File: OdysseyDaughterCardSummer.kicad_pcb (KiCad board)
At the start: 2 copper layers, 47.8 x 46.6 mm, 27 parts, among them J1 Conn_01x01, J2 Conn_01x01, J3 Conn_01x01, J4 Conn_01x01, X1 OdysseyDaughterCard

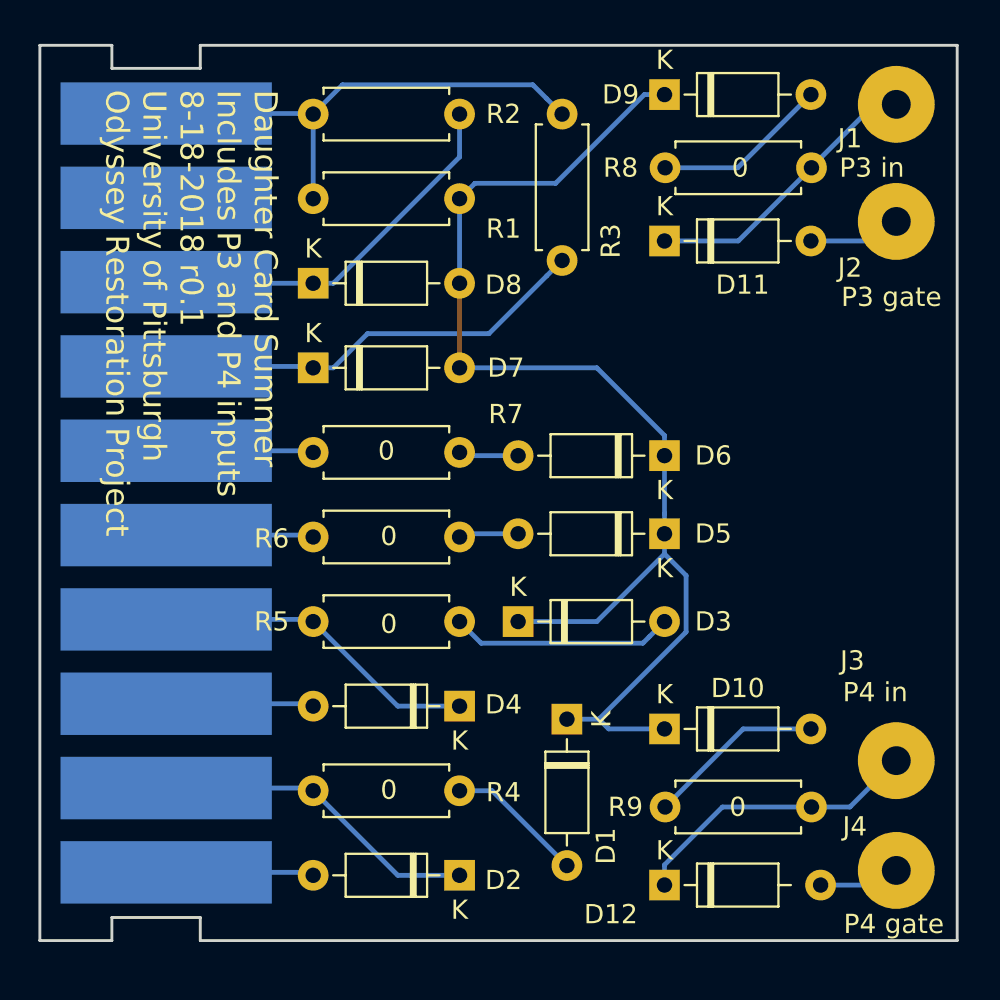
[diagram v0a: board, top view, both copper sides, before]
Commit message: R1.0 remove extra player hardware and replace with single port
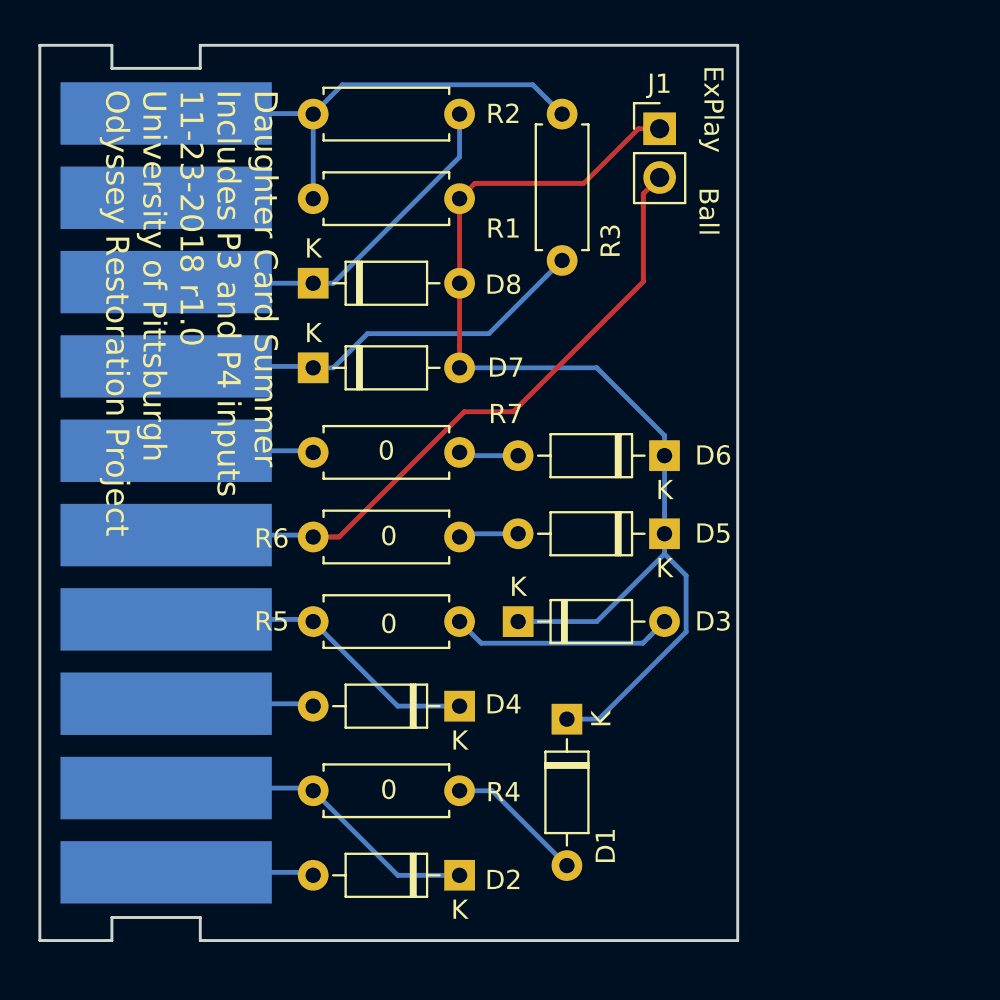
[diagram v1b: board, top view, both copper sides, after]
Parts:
- removed ?: , 
- removed D10, D9: 1N4448, Diode_THT:D_DO-35_SOD27_P7.62mm_Horizontal
- removed D11, D12: BAT83S, Diode_THT:D_DO-35_SOD27_P7.62mm_Horizontal
- removed J2, J3, J4: Conn_01x01, Connector_Wire:SolderWirePad_single_1-5mmDrill
- removed R8, R9: 0, Resistor_THT:R_Axial_DIN0207_L6.3mm_D2.5mm_P7.62mm_Horizontal
- J1: value Conn_01x01 -> Conn_01x02; footprint Connector_Wire:SolderWirePad_single_1-5mmDrill -> Connector_PinHeader_2.54mm:PinHeader_1x02_P2.54mm_Vertical
- moved J1 12.4 mm to (154.7, 82.0)
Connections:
- J1 pad 1: Net-(D11-Pad1) -> Net-(D1-Pad1)
- X1 pad 9: /Card9 -> (no net)
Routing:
- net /Card5: track 7.69 -> 36.2 mm
- net Net-(D12-Pad1): track 15.4 -> 0.00 mm
- net Net-(D11-Pad1): track 15.0 -> 0.00 mm
- net Net-(D10-Pad2): track 9.27 -> 0.00 mm
- net Net-(D9-Pad2): track 9.17 -> 0.00 mm
- net Net-(D11-Pad2): track 4.87 -> 0.00 mm
- net Net-(D1-Pad1): track 65.3 -> 60.7 mm
- net Net-(D12-Pad2): track 4.26 -> 0.00 mm
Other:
- board size 47.8 x 46.6 mm -> 36.3 x 46.6 mm
- board text added: "Ball"
- board text added: "Daughter Card Summer Includes P3 and P4 inputs 11-23-2018 r1.0 University of Pittsburgh Odyssey Restoration Project"
- board text added: "ExPlay"
- board text removed: "Daughter Card Summer Includes P3 and P4 inputs 8-18-2018 r0.1 University of Pittsburgh Odyssey Restoration Project"
- board text removed: "P3 gate"
- board text removed: "P3 in"
- board text removed: "P4 gate"
- board text removed: "P4 in"

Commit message: R1.1 gerbs and board NTSC generator
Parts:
- added C1: 0.1u, Capacitor_THT:C_Disc_D3.8mm_W2.6mm_P2.50mm, F.Cu at (147.8, 106.9)
- added J2: Conn_01x02, Connector_PinHeader_2.54mm:PinHeader_1x02_P2.54mm_Vertical, F.Cu at (165.6, 90.2)
- added J3: Conn_Coaxial, Connector_PinHeader_2.54mm:PinHeader_1x02_P2.54mm_Vertical, F.Cu at (165.6, 118.0)
- added R10: 4.7k, Resistor_THT:R_Axial_DIN0207_L6.3mm_D2.5mm_P7.62mm_Horizontal, F.Cu at (156.7, 90.2)
- added R11: 1k, Resistor_THT:R_Axial_DIN0207_L6.3mm_D2.5mm_P7.62mm_Horizontal, F.Cu at (156.7, 85.6)
- added R12: 75, Resistor_THT:R_Axial_DIN0207_L6.3mm_D2.5mm_P7.62mm_Horizontal, F.Cu at (165.6, 113.0)
- added R8: 100k, Resistor_THT:R_Axial_DIN0207_L6.3mm_D2.5mm_P7.62mm_Horizontal, F.Cu at (159.5, 101.1)
- added R9: 100k, Resistor_THT:R_Axial_DIN0207_L6.3mm_D2.5mm_P7.62mm_Horizontal, F.Cu at (156.7, 120.8)
- added U1: TLV3542, Package_SO:SOIC-8_3.9x4.9mm_P1.27mm, F.Cu at (152.7, 105.7)
- R4: value 0 -> 4.7k
- R5: value 0 -> 820
- R6, R7: value 0 -> 33k
- moved R7 26.4 mm to (156.7, 116.1), turned to 180 degrees
- moved R4 22.3 mm to (149.1, 98.0)
- moved R6 21.9 mm to (156.7, 112.0), turned to 180 degrees
- moved R5 18.1 mm to (149.1, 94.5)
- moved J1 11.0 mm to (165.6, 81.2)
- moved D3 10.8 mm to (136.5, 106.7)
- moved D6 10.8 mm to (144.1, 98.4)
- moved D5 10.8 mm to (144.1, 103.1)
- moved R3 10.6 mm to (156.7, 81.0), turned to 180 degrees
- moved D1 6.66 mm to (144.1, 116.2), turned to 180 degrees
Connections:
- D1 pad 2: Net-(D1-Pad2) -> /Card2
- D3 pad 2: Net-(D3-Pad2) -> /Card4
- D5 pad 2: Net-(D5-Pad2) -> /Card5
- D6 pad 2: Net-(D6-Pad2) -> /Card6
- D7 pad 1: /Card7 -> Net-(D7-Pad1)
- R3 pad 1: /Card7 -> Net-(D7-Pad1)
- R4 pad 1: /Card2 -> Net-(R4-Pad1)
- R4 pad 2: Net-(D1-Pad2) -> VCC
- R5 pad 1: /Card4 -> GND
- R5 pad 2: Net-(D3-Pad2) -> Net-(R4-Pad1)
- R6 pad 1: /Card5 -> Net-(R6-Pad1)
- R6 pad 2: Net-(D5-Pad2) -> /Card10
- R7 pad 1: /Card6 -> Net-(R7-Pad1)
- R7 pad 2: Net-(D6-Pad2) -> Net-(R4-Pad1)
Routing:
- net GND: track 0.00 -> 69.8 mm
- net Net-(D7-Pad1): track 0.00 -> 48.5 mm
- net VCC: track 0.00 -> 36.1 mm
- net Net-(R4-Pad1): track 0.00 -> 30.1 mm
- net /Card10: track 26.3 -> 55.8 mm
- net Net-(R12-Pad2): track 0.00 -> 27.4 mm
- net Net-(R10-Pad2): track 0.00 -> 24.0 mm
- net Net-(R7-Pad1): track 0.00 -> 23.6 mm
- net Net-(R6-Pad1): track 0.00 -> 12.6 mm
- net Net-(D3-Pad2): track 11.6 -> 0.00 mm
- net /Card5: track 36.2 -> 45.1 mm
- net /Card7: track 23.0 -> 30.2 mm, vias 0 -> 1
- net Net-(D1-Pad2): track 7.20 -> 0.00 mm
- net /Card4: track 17.1 -> 22.6 mm
- net Net-(J3-Pad1): track 0.00 -> 4.92 mm
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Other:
- board size 36.3 x 46.6 mm -> 46.5 x 46.6 mm
- board text added: "Daughter Card Summer Includes P3/4 inputs and NTSC generator 2-6-2019 r1.1 University of Pittsburgh Odyssey Restoration Project"
- board text added: "GND"
- board text added: "Vcc"
- board text added: "Video"
- board text removed: "Daughter Card Summer Includes P3 and P4 inputs 11-23-2018 r1.0 University of Pittsburgh Odyssey Restoration Project"

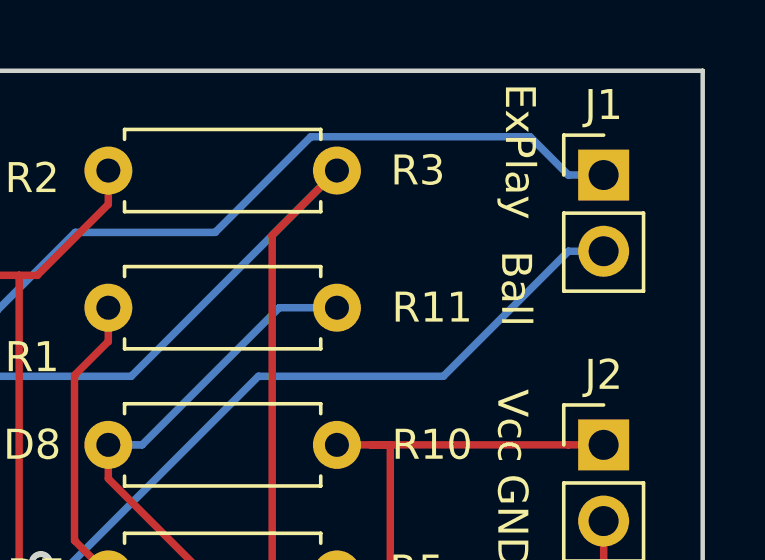
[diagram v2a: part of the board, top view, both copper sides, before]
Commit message: Matt added pad to expansion header on 05-22-20
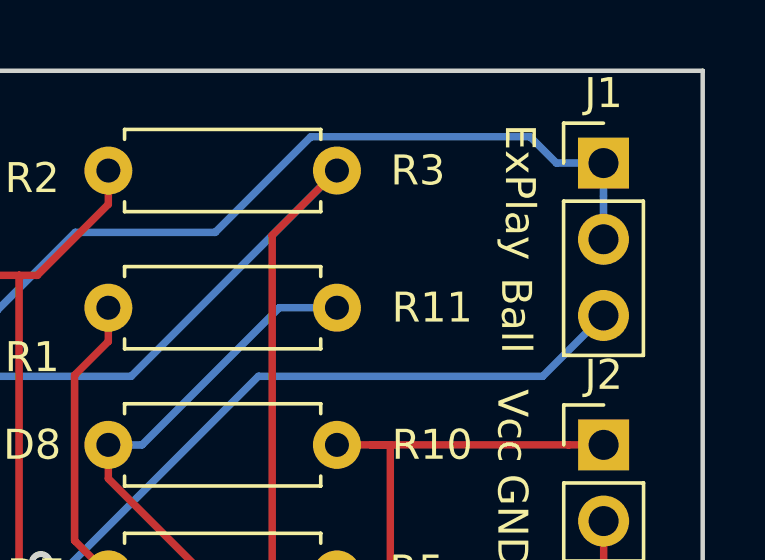
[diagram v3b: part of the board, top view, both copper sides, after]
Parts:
- J1: value Conn_01x02 -> Conn_01x03; footprint Connector_PinHeader_2.54mm:PinHeader_1x02_P2.54mm_Vertical -> Connector_PinHeader_2.54mm:PinHeader_1x03_P2.54mm_Vertical
- moved J1 0.40 mm to (165.6, 80.8)
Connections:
- J1 pad 2: /Card5 -> Net-(D1-Pad1)
- X1 pad 9: (no net) -> /Card9
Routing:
- net Net-(D1-Pad1): track 62.3 -> 64.7 mm
- net /Card5: track 45.1 -> 44.2 mm
